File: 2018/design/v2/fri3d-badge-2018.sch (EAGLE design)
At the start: 1 part

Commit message: completed draft of schematic for prototype 2
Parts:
- added A, B, D, R: SWITCH-MOMENTARY-4.5MM, switches:SWITCH-MOMENTARY-4.5MM
- added ACCELEROMETER: ADXL345BCCZ, ic:ADXL345BCCZ
- added C1, C2: 10uF, passive:CAP0805
- added C10: 4.7uF, passive:CAP0805
- added C11, C3, C9: 0.1uF, passive:CAP0805
- added C12, C13: 22uF, passive:CAP0805
- added C4, C5: 1uF, passive:CAP0805
- added C6, C7: 47pF, passive:CAP0805
- added C8: 0.01uF, passive:CAP0805
- added CHARGE: TP4056, power:TP4056
- added DUAL_MOSFET: FS8205A, ic:FS8205A
- added GREEN, LED1, LED10, LED11, LED12, LED13, LED14, LED15, LED16, LED17, LED18, LED19, LED2, LED20, LED21, LED22, LED23, LED24, LED25, LED26, LED27, LED28, LED29, LED3, LED30, LED31, LED32, LED33, LED34, LED35, LED4, LED5, LED6, LED7, LED8, LED9, RED: (no value), led:LEDCHIP-LED0805
- added J1: (no value), SparkFun-Connectors:CONN_06SILK_FEMALE_PTH
- added L1: INDUCTOR-0805-3.3UH, SparkFun-Coils:INDUCTOR-0805-3.3UH
- added L2: 10uH, passive:INDUCTOR0805
- added LDO: XC6210, power:XC6210
- added MCU: ESP-WROOM-32, esp32:ESP-WROOM-32
- added PROTECT: DW01-P, power:DW01-P
- added R1, R2, R7: 1K, passive:RESISTOR0805-RES
- added R10, R11, R8, R9: 10K, passive:RESISTOR0805-RES
- added R12: 82K, passive:RESISTOR0805-RES
- added R13: 11K, passive:RESISTOR0805-RES
- added R14, R15, R16, R17, R18, R19, R20, R21, R22, R23, R24, R25, R26, R27: (no value), passive:RESISTOR0805-RES
- added R28: 0, passive:RESISTOR0805-RES
- added R3, R4: 27, passive:RESISTOR0805-RES
- added R5: 1.2K, passive:RESISTOR0805-RES
- added R6: 100, passive:RESISTOR0805-RES
- added RIGHT_EYE: 5x7 LED DOT MATRIX, led:5X7_DOT_LED_MATRIX
- added SHIFT1, SHIFT2, SHIFT3: 74HC595, ic:74HC595
- added STEP-UP: SX1308, power:SX1308
- added U$3: CR18650, setup:CR18650
- added U$7: SLIDE_DPDT, switches:SLIDE_DPDT
- added USB: USB_MICRO_B, connector:USB_MICRO_B
- added USB-TTL: FT234XD, ftdi-chip:FT234XD
- U$1: value USB_MICRO_B -> SCHOTTKY; device connector:USB_MICRO_B -> passive:SCHOTTKY
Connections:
- new net 3V3: A.2, ACCELEROMETER.VCC, ACCELEROMETER.VS, B.2, C5.1, LDO.VOUT, MCU.3V3, R8.2, R9.2, SHIFT1.!SCLR, SHIFT1.VCC, SHIFT2.!SCLR, SHIFT2.VCC, SHIFT3.!SCLR, SHIFT3.VCC
- new net 5V: U$7.5
- new net 5V_ENABLE: STEP-UP.EN
- new net ACC_ENABLE: ACCELEROMETER.!CS!
- new net ACC_INT1: ACCELEROMETER.INT1
- new net ACC_INT2: ACCELEROMETER.INT2
- new net ACC_MISO: ACCELEROMETER.SDO/ALT-ADDR
- new net ACC_MOSI: ACCELEROMETER.SDA/SDI/SDIO
- new net ACC_SCK: ACCELEROMETER.SCL/SCLK
- new net BUTTON-A: B.1, R10.2
- new net BUTTON-B: A.1, R11.2
- new net D+: C6.1, R4.1, USB.D+
- new net D-: C7.1, R3.1, USB.D-
- new net DOWNLOAD: D.1, MCU.IO0, R9.1
- new net GND: ACCELEROMETER.GND@1, ACCELEROMETER.GND@2, ACCELEROMETER.GND@3, C1.2, C10.2, C11.2, C12.2, C13.2, C2.2, C4.2, C5.2, C6.2, C7.2, C8.2, C9.2, CHARGE.GND, CHARGE.TEMP, D.2, DUAL_MOSFET.S2@1, DUAL_MOSFET.S2@2, J1.1, LDO.GND, MCU.GND@1, MCU.GND@2, MCU.GND@3, R.2, R10.1, R11.1, R13.1, R28.1, R5.1, R7.2, SHIFT1.GND, SHIFT2.GND, SHIFT3.GND, STEP-UP.GND, USB-TTL.GND@13, USB-TTL.GND@5, USB.GND
- new net LC1: R14.1
- new net LC2: R15.1
- new net LC3: R16.1
- new net LC4: R17.1
- new net LC5: R18.1
- new net LC6: R19.1
- new net LC7: R20.1
- new net LEDS_ENABLE: SHIFT1.!G, SHIFT2.!G, SHIFT3.!G
- new net LEDS_RCK: SHIFT1.RCK, SHIFT2.RCK, SHIFT3.RCK
- new net LEDS_SCK: SHIFT1.SCK, SHIFT2.SCK, SHIFT3.SCK
- new net LEDS_SIN: SHIFT1.SIN
- new net LR1: LED1.A, LED2.A, LED3.A, LED4.A, LED5.A, LED6.A, LED7.A
- new net LR2: LED10.A, LED11.A, LED12.A, LED13.A, LED14.A, LED8.A, LED9.A
- new net LR3: LED15.A, LED16.A, LED17.A, LED18.A, LED19.A, LED20.A, LED21.A
- new net LR4: LED22.A, LED23.A, LED24.A, LED25.A, LED26.A, LED27.A, LED28.A
- new net LR5: LED29.A, LED30.A, LED31.A, LED32.A, LED33.A, LED34.A, LED35.A
- new net N$10: CHARGE.PROG, R5.2
- new net N$11: C3.2, DUAL_MOSFET.S1@1, DUAL_MOSFET.S1@2, PROTECT.GND, R28.2, U$3.-
- new net N$12: PROTECT.CS, R7.1
- new net N$13: C3.1, PROTECT.VCC, R6.2
- new net N$14: DUAL_MOSFET.G1, PROTECT.OD
- new net N$15: DUAL_MOSFET.G2, PROTECT.OC
- new net N$18: R12.1, R13.2, STEP-UP.FB
- new net N$19: L2.2, STEP-UP.SW, U$1.A
- new net N$20: SHIFT1.SOUT, SHIFT2.SIN
- new net N$21: SHIFT2.SOUT, SHIFT3.SIN
- new net N$22: SHIFT1.QH
- new net N$23: SHIFT1.QG
- new net N$24: SHIFT1.QF
- new net N$25: SHIFT1.QE
- new net N$26: SHIFT1.QA
- new net N$27: SHIFT1.QB
- new net N$28: SHIFT1.QC
- new net N$29: SHIFT1.QD
- new net N$3: R3.2, USB-TTL.USBDM
- new net N$30: R21.1, RIGHT_EYE.R1
- new net N$31: R22.1, RIGHT_EYE.R2
- new net N$32: LED1.C, LED15.C, LED22.C, LED29.C, LED8.C, R14.2
- new net N$33: LED16.C, LED2.C, LED23.C, LED30.C, LED9.C, R15.2
- new net N$34: LED10.C, LED17.C, LED24.C, LED3.C, LED31.C, R16.2
- new net N$35: LED11.C, LED18.C, LED25.C, LED32.C, LED4.C, R17.2
- new net N$36: LED12.C, LED19.C, LED26.C, LED33.C, LED5.C, R18.2
- new net N$37: LED13.C, LED20.C, LED27.C, LED34.C, LED6.C, R19.2
- new net N$38: LED14.C, LED21.C, LED28.C, LED35.C, LED7.C, R20.2
- new net N$39: R24.1, RIGHT_EYE.R4
- new net N$4: CHARGE.!CHRG!, R1.1
- new net N$40: R23.1, RIGHT_EYE.R3
- new net N$41: R25.1, RIGHT_EYE.R5
- new net N$42: R26.1, RIGHT_EYE.R6
- new net N$43: R27.1, RIGHT_EYE.R7
- new net N$44: SHIFT2.QH
- new net N$45: SHIFT2.QG
- new net N$46: SHIFT2.QF
- new net N$47: SHIFT2.QE
- new net N$48: SHIFT2.QA
- new net N$49: SHIFT2.QB
- new net N$5: R4.2, USB-TTL.USBDP
- new net N$50: SHIFT2.QC
- new net N$51: SHIFT2.QD
- new net N$52: SHIFT3.QH
- new net N$53: SHIFT3.QG
- new net N$54: SHIFT3.QF
- new net N$55: SHIFT3.QE
- new net N$56: SHIFT3.QA
- new net N$57: SHIFT3.QB
- new net N$58: SHIFT3.QC
- new net N$59: SHIFT3.QD
- new net N$6: C9.1, USB-TTL.!RESET!, USB-TTL.3V3OUT, USB-TTL.VCCIO
- new net N$7: CHARGE.!STDBY!, R2.1
- new net N$8: R1.2, RED.C
- new net N$9: GREEN.C, R2.2
- new net RC1: R21.2
- new net RC2: R22.2
- new net RC3: R23.2
- new net RC4: R24.2
- new net RC5: R25.2
- new net RC6: R26.2
- new net RC7: R27.2
- new net RESET: MCU.EN, R.1, R8.1
- new net RR1: RIGHT_EYE.C1
- new net RR2: RIGHT_EYE.C2
- new net RR3: RIGHT_EYE.C3
- new net RR4: RIGHT_EYE.C4
- new net RR5: RIGHT_EYE.C5
- new net RX: J1.4, MCU.RXD0, USB-TTL.TXD
- new net TX: J1.5, MCU.TXD0, USB-TTL.RXD
- new net USB-RAW: C8.1, L1.1, USB.VBUS
- new net VBAT: C1.1, CHARGE.BAT, R6.1, U$3.+, U$7.3
- new net VCC: C12.1, C4.1, L2.1, LDO.CE, LDO.VIN, STEP-UP.IN, U$7.2
- new net VSTEPUP: C13.1, R12.2, U$1.C, U$7.6
- new net VUSB: C10.1, C11.1, C2.1, CHARGE.CE, CHARGE.VCC, GREEN.A, L1.2, RED.A, U$7.1, U$7.4, USB-TTL.VCC
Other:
- note added: "3V3"
- note added: "5V"
- note added: "5V = 0.6 (Vref) * ( 1 + R1 / R2 )"
- note added: "A"
- note added: "ACCELEROMETER"
- note added: "B"
- note added: "BATTERY"
- note added: "Battery + Protection"
- note added: "Buttons"
- note added: "CHARGE"
- note added: "Charger"
- note added: "DNF"
- note added: "FTDI CABLE"
- note added: "LDO"
- note added: "LED ARRAY LEFT EYE"
- note added: "LED ARRAY RIGHT EYE"
- note added: "MCU"
- note added: "POWER SWITCH"
- note added: "R1 / R2 = 7.333"
- note added: "SHIFT REGISTERS"
- note added: "STEP UP"
- note added: "SWITCH"
- note added: "Structure"
- note added: "USB"
- note added: "USB RAW"
- note added: "USB connector"
- note added: "USB-TTL"
- note added: "VBAT"
- note added: "VCC"
- note added: "VSTEPUP"
- note added: "VUSB"

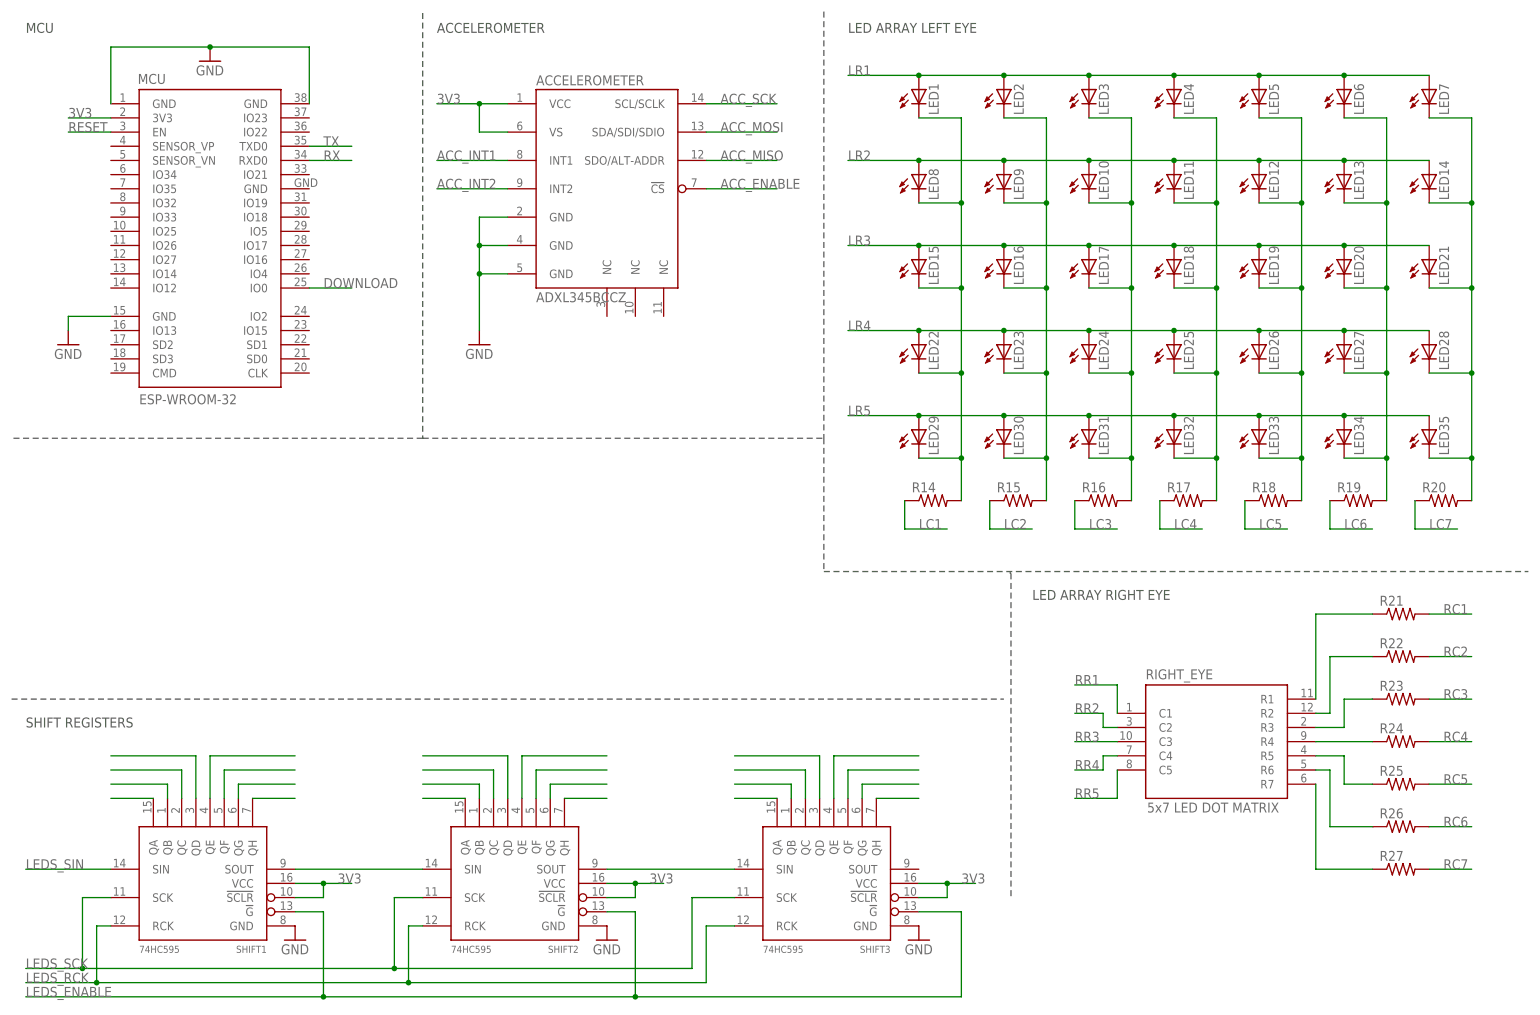
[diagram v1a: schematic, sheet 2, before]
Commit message: added extension headers + expansion board
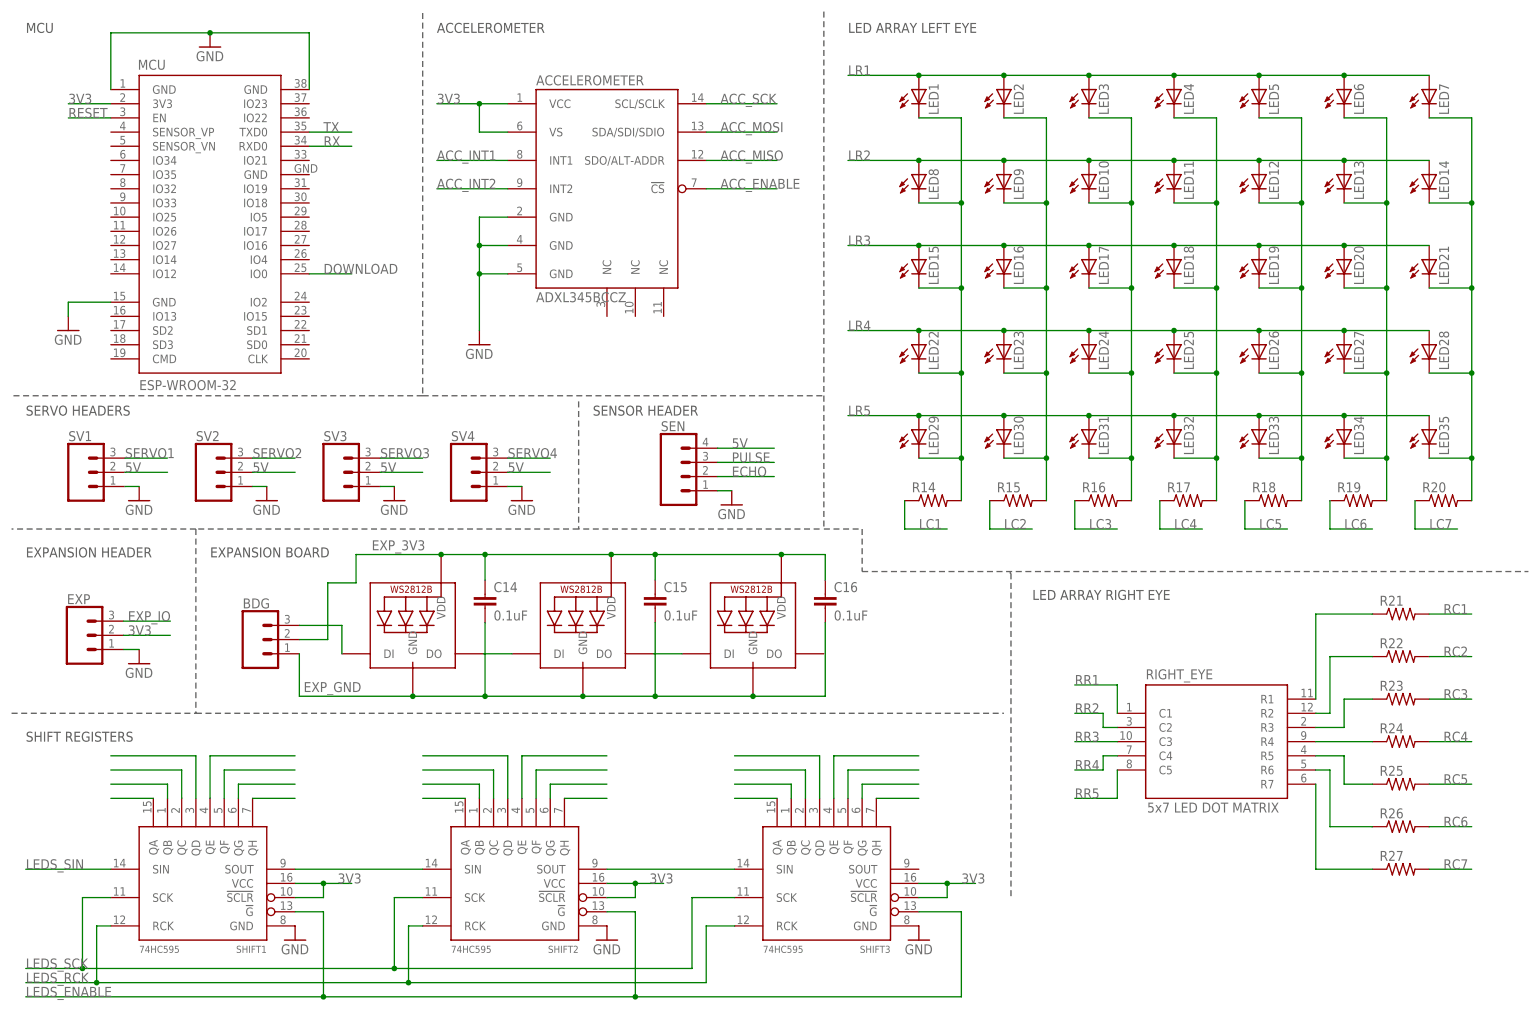
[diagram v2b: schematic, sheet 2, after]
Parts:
- added BDG, EXP, SV1, SV2, SV3, SV4: (no value), SparkFun-Connectors:CONN_03
- added C14, C15, C16: 0.1uF, passive:CAP0805
- added SEN: (no value), SparkFun-Connectors:CONN_04
- added WS1, WS2, WS3: WS2812B5050, adafruit:WS2812B5050
- renumbered J1 to FTDI, U$7 to PWR
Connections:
- new net ECHO: SEN.2
- new net EXP_3V3: BDG.2, C14.1, C15.1, C16.1, WS1.VDD, WS2.VDD, WS3.VDD
- new net EXP_GND: BDG.1, C14.2, C15.2, C16.2, WS1.GND, WS2.GND, WS3.GND
- new net EXP_IO: EXP.3
- new net N$17: WS1.DO, WS2.DI
- new net N$60: WS2.DO, WS3.DI
- new net N$61: BDG.3, WS1.DI
- new net PULSE: SEN.3
- new net SERVO1: SV1.3
- new net SERVO2: SV2.3
- new net SERVO3: SV3.3
- new net SERVO4: SV4.3
- net 3V3: now also EXP.2
- net 5V: now also SEN.4, SV1.2, SV2.2, SV3.2, SV4.2
- net GND: now also EXP.1, SEN.1, SV1.1, SV2.1, SV3.1, SV4.1
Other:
- note added: "EXPANSION BOARD"
- note added: "EXPANSION HEADER"
- note added: "SENSOR HEADER"
- note added: "SERVO HEADERS"
- moved on the sheet: MCU

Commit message: completed first layout prototype 2
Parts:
- added C17, C18, C19: 1uF, passive:CAP0805
- added D1: SCHOTTKY, passive:SCHOTTKY
- added LDO_MCU: XC6210, power:XC6210
- added Q1: (no value), mosfet:MOSFET-NREFLOW
- added R29: 0, passive:RESISTOR0805-RES
- added R30: 240, passive:RESISTOR0805-RES
- added R31, R32: 10K, passive:RESISTOR0805-RES
- added R33: 1K, passive:RESISTOR0805-RES
- R14, R15, R16, R17, R18, R19, R20, R21, R22, R23, R24, R25, R26, R27: value (none) -> 100
- U$1: value SCHOTTKY -> KLJ-1230; device passive:SCHOTTKY -> sound:KLJ-1230
- renumbered ACCELEROMETER to ACC
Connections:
- removed net EXP_3V3: BDG.2, C14.1, C15.1, C16.1, WS1.VDD, WS2.VDD, WS3.VDD
- removed net N$22: SHIFT1.QH
- removed net N$23: SHIFT1.QG
- removed net N$24: SHIFT1.QF
- removed net N$25: SHIFT1.QE
- removed net N$26: SHIFT1.QA
- removed net N$27: SHIFT1.QB
- removed net N$28: SHIFT1.QC
- removed net N$29: SHIFT1.QD
- removed net N$44: SHIFT2.QH
- removed net N$45: SHIFT2.QG
- removed net N$46: SHIFT2.QF
- removed net N$47: SHIFT2.QE
- removed net N$48: SHIFT2.QA
- removed net N$49: SHIFT2.QB
- removed net N$50: SHIFT2.QC
- removed net N$51: SHIFT2.QD
- removed net N$52: SHIFT3.QH
- removed net N$53: SHIFT3.QG
- removed net N$54: SHIFT3.QF
- removed net N$55: SHIFT3.QE
- removed net N$56: SHIFT3.QA
- removed net N$57: SHIFT3.QB
- removed net N$58: SHIFT3.QC
- removed net N$59: SHIFT3.QD
- new net 3V3_MCU: C18.1, LDO_MCU.VOUT, MCU.3V3
- new net BUZZER: MCU.IO13, R30.1
- new net EXP_5V: C14.1, C15.1, C16.1, R29.2, WS1.VDD, WS2.VDD, WS3.VDD
- new net N$11: Q1.G, R30.2, R32.2
- new net N$16: BDG.2, R29.1
- new net N$2: Q1.D, R33.1, U$1.-
- new net N$63: Q1.S, R31.1
- net 3V3: now also R33.2, U$1.+; no longer EXP.2, MCU.3V3
- net 5V: now also EXP.2
- net 5V_ENABLE: now also MCU.SD1
- net ACC_ENABLE: now also MCU.IO27
- net ACC_INT1: now also MCU.IO26
- net ACC_INT2: now also MCU.IO25
- net ACC_MISO: now also MCU.IO33
- net ACC_MOSI: now also MCU.IO32
- net ACC_SCK: now also MCU.IO35
- net BUTTON-A: now also MCU.IO4
- net BUTTON-B: now also MCU.IO12
- net ECHO: now also MCU.IO5
- net EXP_IO: now also MCU.IO16
- net GND: now also C17.2, C18.2, C19.1, LDO_MCU.GND, R31.2, R32.1
- net LC1: now also SHIFT3.QH
- net LC2: now also SHIFT3.QG
- net LC3: now also SHIFT3.QF
- net LC4: now also SHIFT3.QE
- net LC5: now also SHIFT3.QD
- net LC6: now also SHIFT3.QC
- net LC7: now also SHIFT3.QB
- net LEDS_RCK: now also C19.2
- net LEDS_SIN: now also MCU.IO14
- net LR1: now also SHIFT2.QH
- net LR2: now also SHIFT2.QG
- net LR3: now also SHIFT2.QF
- net LR4: now also SHIFT2.QE
- net LR5: now also SHIFT3.QA
- net N$19: now also D1.A; no longer U$1.A
- net PULSE: now also MCU.IO17
- net RC1: now also SHIFT1.QE
- net RC2: now also SHIFT1.QD
- net RC3: now also SHIFT1.QH
- net RC4: now also SHIFT1.QF
- net RC5: now also SHIFT1.QC
- net RC6: now also SHIFT1.QB
- net RC7: now also SHIFT1.QA
- net RR1: now also SHIFT1.QG
- net RR2: now also SHIFT2.QB
- net RR3: now also SHIFT2.QC
- net RR4: now also SHIFT2.QA
- net RR5: now also SHIFT2.QD
- net SERVO1: now also MCU.IO15
- net SERVO2: now also MCU.IO2
- net SERVO3: now also MCU.IO19
- net SERVO4: now also MCU.IO18
- net VCC: now also C17.1, LDO_MCU.CE, LDO_MCU.VIN
- net VSTEPUP: now also D1.C; no longer U$1.C
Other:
- note added: "0Ohm or diode"
- note added: "3V3_MCU"
- note added: "Buzzer"
- note added: "LDO_MCU"
- moved on the sheet: C4, C5, FTDI, LDO, PWR, R28, USB
